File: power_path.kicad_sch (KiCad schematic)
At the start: 36 parts, among them J2 USB_C_Receptacle_USB2.0_16P, SW1 SW_SPST, U2 TPS631000DRLR, U3 TLV77018PDBVR, U4 TPS2116DRL, U5 USBLC6-2SC6, U6 USBLC6-2SC6, U7 BQ25302, U8 BQ27427YZFR

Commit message: random changes
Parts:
- SW1: value SW_SPST -> G-Switch SK-12E12-G060
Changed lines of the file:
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@@
 			)
 		)
-		(property "Datasheet" ""
+		(property "Datasheet" "https://www.ti.com/lit/ds/symlink/bq27427.pdf"
 			(at 246.38 121.92 0)
 			(hide yes)
@@
 			)
 		)
-		(property "Value" "SW_SPST"
+		(property "Value" "G-Switch SK-12E12-G060"
 			(at 203.2 102.87 0)
 			(show_name no)

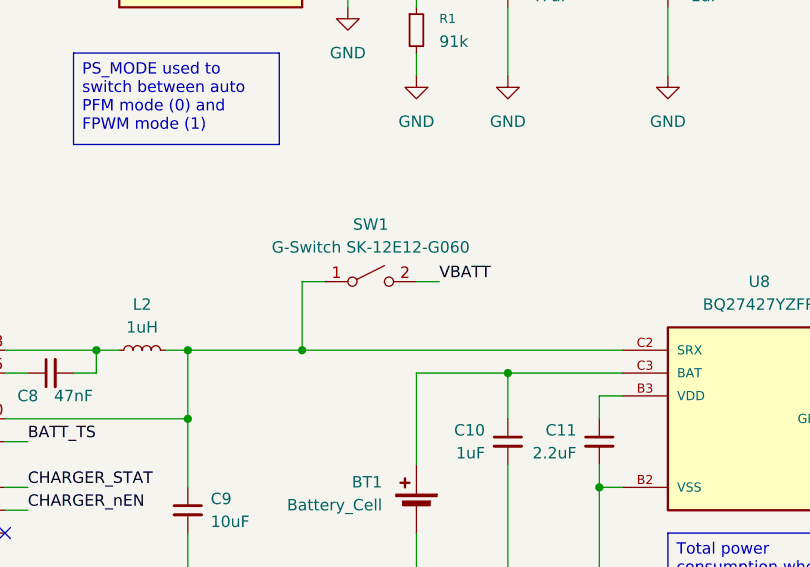
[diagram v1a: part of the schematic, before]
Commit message: rename custom libraries to custom, add easyeda2kicad integration
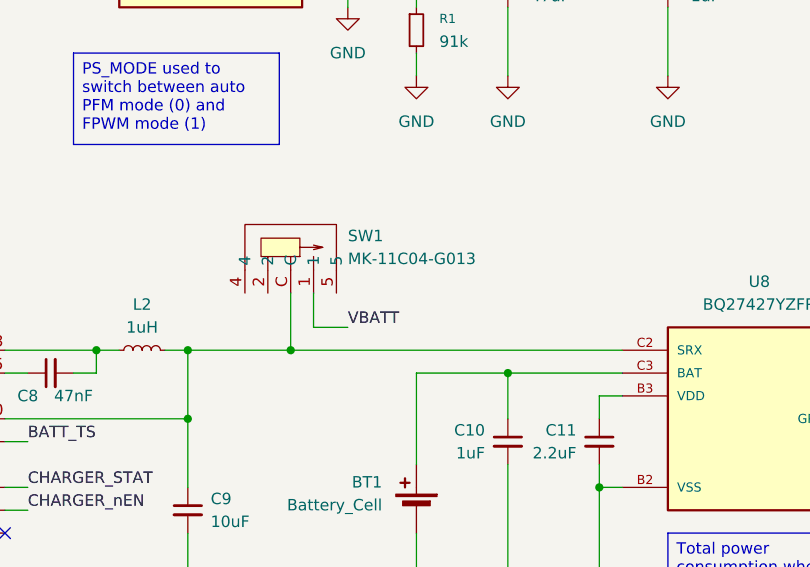
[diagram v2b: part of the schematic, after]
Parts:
- removed SW1: G-Switch SK-12E12-G060, footprints:SK-12E12-G060, symbol Switch:SW_SPST
- added SW1: MK-11C04-G013, custom:SW-SMD_MK-11C04-G013, symbol custom:MK-11C04-G013
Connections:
- net VBATT: now also SW1.1
- net at C9.1, L2.2, U7.10 (BAT)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: now also SW1.C
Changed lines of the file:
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@@
 	)
 	(junction
-		(at 139.7 177.8)
+		(at 194.31 114.3)
 		(diameter 0)
 		(color 0 0 0 0)
 	)
 	(junction
-		(at 99.06 73.66)
+		(at 139.7 177.8)
 		(diameter 0)
 		(color 0 0 0 0)
 	)
 	(junction
-		(at 195.58 114.3)
+		(at 99.06 73.66)
 		(diameter 0)
 		(color 0 0 0 0)
@@
 	(wire
 		(pts
-			(xy 195.58 106.68) (xy 198.12 106.68)
-		)
-		(stroke
-			(width 0)
-			(type default)
-		)
-	)
-	(wire
-		(pts
 			(xy 35.56 157.48) (xy 38.1 157.48)
 		)
@@
 	(wire
 		(pts
-			(xy 208.28 106.68) (xy 210.82 106.68)
+			(xy 236.22 63.5) (xy 243.84 63.5)
 		)
 		(stroke
@@
 	(wire
 		(pts
-			(xy 236.22 63.5) (xy 243.84 63.5)
+			(xy 99.06 71.12) (xy 99.06 73.66)
 		)
 		(stroke
@@
 	(wire
 		(pts
-			(xy 99.06 71.12) (xy 99.06 73.66)
+			(xy 35.56 147.32) (xy 38.1 147.32)
 		)
 		(stroke
@@
 	(wire
 		(pts
-			(xy 35.56 147.32) (xy 38.1 147.32)
+			(xy 68.58 76.2) (xy 68.58 78.74)
 		)
 		(stroke
@@
 	(wire
 		(pts
-			(xy 68.58 76.2) (xy 68.58 78.74)
+			(xy 170.18 68.58) (xy 172.72 68.58)
 		)
 		(stroke
@@
 	(wire
 		(pts
-			(xy 170.18 68.58) (xy 172.72 68.58)
+			(xy 124.46 139.7) (xy 124.46 142.24)
 		)
 		(stroke
@@
 	(wire
 		(pts
-			(xy 124.46 139.7) (xy 124.46 142.24)
+			(xy 196.85 107.95) (xy 196.85 111.76)
 		)
 		(stroke
@@
 	(wire
 		(pts
-			(xy 195.58 106.68) (xy 195.58 114.3)
+			(xy 194.31 107.95) (xy 194.31 114.3)
 		)
 		(stroke
@@
 	(wire
 		(pts
-			(xy 195.58 114.3) (xy 231.14 114.3)
-		)
-		(stroke
-			(width 0)
-			(type default)
-		)
-	)
-	(wire
-		(pts
 			(xy 66.04 68.58) (xy 68.58 68.58)
 		)
@@
 	(wire
 		(pts
-			(xy 182.88 114.3) (xy 195.58 114.3)
+			(xy 200.66 111.76) (xy 196.85 111.76)
+		)
+		(stroke
+			(width 0)
+			(type default)
+		)
+	)
+	(wire
+		(pts
+			(xy 182.88 114.3) (xy 194.31 114.3)
 		)
 		(stroke
@@
 	(wire
 		(pts
+			(xy 194.31 114.3) (xy 231.14 114.3)
+		)
+		(stroke
+			(width 0)
+			(type default)
+		)
+	)
+	(wire
+		(pts
 			(xy 264.16 116.84) (xy 261.62 116.84)
 		)
@@
 	)
 	(label "VBATT"
-		(at 210.82 106.68 0)
+		(at 200.66 111.76 0)
 		(effects
 			(font
@@
 	)
 	(symbol
+		(lib_id "custom:MK-11C04-G013")
+		(at 195.58 104.14 180)
+		(unit 1)
+		(body_style 1)
+		(exclude_from_sim no)
+		(in_bom yes)
+		(on_board yes)
+		(in_pos_files yes)
+		(dnp no)
+		(fields_autoplaced yes)
+		(property "Reference" "SW1"
+			(at 200.66 101.5999 0)
+			(show_name no)
+			(do_not_autoplace no)
+			(effects
+				(font
+					(size 1.27 1.27)
+				)
+				(justify right)
+			)
+		)
+		(property "Value" "MK-11C04-G013"
+			(at 200.66 104.1399 0)
+			(show_name no)
+			(do_not_autoplace no)
+			(effects
+				(font
+					(size 1.27 1.27)
+				)
+				(justify right)
+			)
+		)
+		(property "Footprint" "custom:SW-SMD_MK-11C04-G013"
+			(at 195.58 100.33 0)
+			(hide yes)
+			(show_name no)
+			(do_not_autoplace no)
+			(effects
+				(font
+					(size 1.27 1.27)
+				)
+			)
+		)
+		(property "Datasheet" "https://lcsc.com/product-detail/Toggle-Switches_G-Switch-MK-11C04-G013_C778185.html"
+			(at 195.58 97.79 0)
+			(hide yes)
+			(show_name no)
+			(do_not_autoplace no)
+			(effects
+				(font
+					(size 1.27 1.27)
+				)
+			)
+		)
+		(property "Description" ""
+			(at 195.58 104.14 0)
+			(hide yes)
+			(show_name no)
+			(do_not_autoplace no)
+			(effects
+				(font
+					(size 1.27 1.27)
+				)
+			)
+		)
+		(property "Manufacturer" "G-Switch(品赞)"
+			(at 195.58 95.25 0)
+			(hide yes)
+			(show_name no)
+			(do_not_autoplace no)
+			(effects
+				(font
+					(size 1.27 1.27)
+				)
+			)
+		)
+		(property "MPN" "MK-11C04-G013"
+			(at 195.58 92.71 0)
+			(hide yes)
+			(show_name no)
+			(do_not_autoplace no)
+			(effects
+				(font
+					(size 1.27 1.27)
+				)
+			)
+		)
+		(property "LCSC Part" "C778185"
+			(at 195.58 90.17 0)
+			(hide yes)
+			(show_name no)
+			(do_not_autoplace no)
+			(effects
+				(font
+					(size 1.27 1.27)
+				)
+			)
+		)
+		(property "LCSC" "C778185"
+			(at 195.58 85.09 0)
+			(hide yes)
+			(show_name no)
+			(do_not_autoplace no)
+			(effects
+				(font
+					(size 1.27 1.27)
+				)
+			)
+		)
+		(pin "5"
+		)
+		(pin "1"
+		)
+		(pin "4"
+		)
+		(pin "2"
+		)
+		(pin "C"
+		)
+		(instances
+			(project "pedal"
+				(path "/e2443317-b83f-4e66-ac79-3186c6d613f3/487ab5a8-1c1d-4a3e-8f62-a21afc38e9a3"
+					(reference "SW1")
+					(unit 1)
+				)
+			)
+		)
+	)
+	(symbol
 		(lib_id "Device:R_Small")
 		(at 274.32 121.92 90)
@@
 					(unit 1)
 				)
-			)
-		)
-	)
-	(symbol
-		(lib_id "Switch:SW_SPST")
-		(at 203.2 106.68 0)
-		(unit 1)
-		(body_style 1)
-		(exclude_from_sim no)
-		(in_bom yes)
-		(on_board yes)
-		(in_pos_files yes)
-		(dnp no)
-		(fields_autoplaced yes)
-		(property "Reference" "SW1"
-			(at 203.2 100.33 0)
-			(show_name no)
-			(do_not_autoplace no)
-			(effects
-				(font
-					(size 1.27 1.27)
-				)
-			)
-		)
-		(property "Value" "G-Switch SK-12E12-G060"
-			(at 203.2 102.87 0)
-			(show_name no)
-			(do_not_autoplace no)
-			(effects
-				(font
-					(size 1.27 1.27)
-				)
-			)
-		)
-		(property "Footprint" "footprints:SK-12E12-G060"
-			(at 203.2 106.68 0)
-			(hide yes)
-			(show_name no)
-			(do_not_autoplace no)
-			(effects
-				(font
-					(size 1.27 1.27)
-				)
-			)
-		)
-		(property "Datasheet" ""
-			(at 203.2 106.68 0)
-			(hide yes)
-			(show_name no)
-			(do_not_autoplace no)
-			(effects
-				(font
-					(size 1.27 1.27)
-				)
-			)
-		)
-		(property "Description" "Single Pole Single Throw (SPST) switch"
-			(at 203.2 106.68 0)
-			(hide yes)
-			(show_name no)
-			(do_not_autoplace no)
-			(effects
-				(font
-					(size 1.27 1.27)
-				)
-			)
-		)
-		(property "LCSC" "C22448008"
-			(at 203.2 106.68 0)
-			(hide yes)
-			(show_name no)
-			(do_not_autoplace no)
-			(effects
-				(font
-					(size 1.27 1.27)
-				)
-			)
-		)
-		(pin "1"
-		)
-		(pin "2"
-		)
-		(pin "3"
-		)
-		(pin "M"
-		)
-		(instances
-			(project "pedal"
-				(path "/e2443317-b83f-4e66-ac79-3186c6d613f3/487ab5a8-1c1d-4a3e-8f62-a21afc38e9a3"
-					(reference "SW1")
-					(unit 1)
-				)

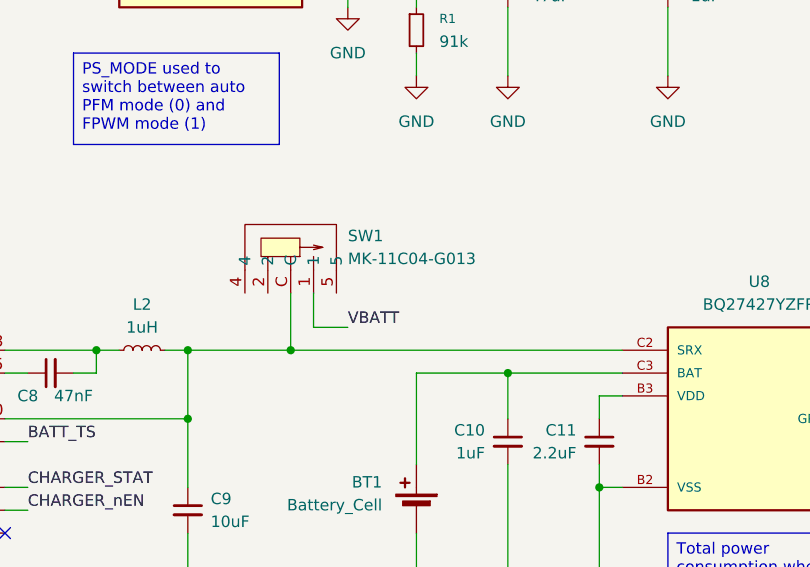
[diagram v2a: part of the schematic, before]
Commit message: move switch to be on grid
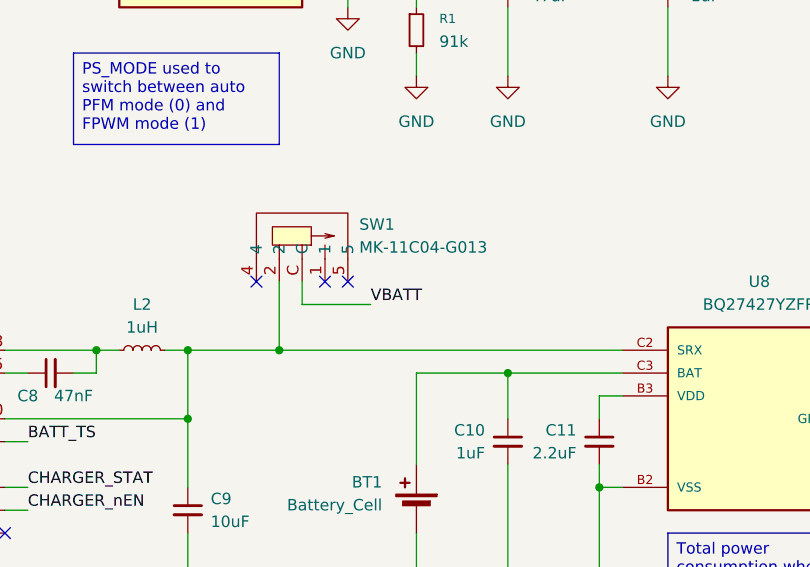
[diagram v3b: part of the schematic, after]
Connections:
- net VBATT: now also SW1.C; no longer SW1.1
- net at C9.1, L2.2, U7.10 (BAT)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: now also SW1.2; no longer SW1.C
- no-connect marks 2 -> 5
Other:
- moved on the sheet: SW1
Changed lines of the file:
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@@
 	)
 	(junction
-		(at 154.94 63.5)
+		(at 193.04 114.3)
 		(diameter 0)
 		(color 0 0 0 0)
 	)
 	(junction
-		(at 208.28 63.5)
+		(at 154.94 63.5)
 		(diameter 0)
 		(color 0 0 0 0)
 	)
 	(junction
-		(at 149.86 142.24)
+		(at 208.28 63.5)
 		(diameter 0)
 		(color 0 0 0 0)
 	)
 	(junction
-		(at 172.72 114.3)
+		(at 149.86 142.24)
 		(diameter 0)
 		(color 0 0 0 0)
 	)
 	(junction
-		(at 194.31 114.3)
+		(at 172.72 114.3)
 		(diameter 0)
 		(color 0 0 0 0)
@@
 		(at 162.56 134.62)
 	)
+	(no_connect
+		(at 190.5 106.68)
+	)
+	(no_connect
+		(at 200.66 106.68)
+	)
+	(no_connect
+		(at 198.12 106.68)
+	)
 	(wire
 		(pts
@@
 	(wire
 		(pts
-			(xy 196.85 107.95) (xy 196.85 111.76)
+			(xy 195.58 106.68) (xy 195.58 109.22)
 		)
 		(stroke
@@
 	(wire
 		(pts
-			(xy 194.31 107.95) (xy 194.31 114.3)
+			(xy 193.04 106.68) (xy 193.04 114.3)
 		)
 		(stroke
@@
 	(wire
 		(pts
-			(xy 200.66 111.76) (xy 196.85 111.76)
+			(xy 203.2 109.22) (xy 195.58 109.22)
 		)
 		(stroke
@@
 	(wire
 		(pts
-			(xy 182.88 114.3) (xy 194.31 114.3)
+			(xy 182.88 114.3) (xy 193.04 114.3)
 		)
 		(stroke
@@
 	(wire
 		(pts
+			(xy 193.04 114.3) (xy 231.14 114.3)
+		)
+		(stroke
+			(width 0)
+			(type default)
+		)
+	)
+	(wire
+		(pts
 			(xy 124.46 132.08) (xy 124.46 134.62)
 		)
@@
 	(wire
 		(pts
-			(xy 194.31 114.3) (xy 231.14 114.3)
-		)
-		(stroke
-			(width 0)
-			(type default)
-		)
-	)
-	(wire
-		(pts
 			(xy 264.16 116.84) (xy 261.62 116.84)
 		)
@@
 	)
 	(label "VBATT"
-		(at 200.66 111.76 0)
+		(at 203.2 109.22 0)
 		(effects
 			(font
@@
 	(symbol
 		(lib_id "custom:MK-11C04-G013")
-		(at 195.58 104.14 180)
+		(at 196.85 102.87 180)
 		(unit 1)
 		(body_style 1)
@@
 		(fields_autoplaced yes)
 		(property "Reference" "SW1"
-			(at 200.66 101.5999 0)
+			(at 201.93 100.3299 0)
 			(show_name no)
 			(do_not_autoplace no)
@@
 		)
 		(property "Value" "MK-11C04-G013"
-			(at 200.66 104.1399 0)
+			(at 201.93 102.8699 0)
 			(show_name no)
 			(do_not_autoplace no)
@@
 		)
 		(property "Footprint" "custom:SW-SMD_MK-11C04-G013"
-			(at 195.58 100.33 0)
+			(at 196.85 99.06 0)
 			(hide yes)
 			(show_name no)
@@
 		)
 		(property "Datasheet" "https://lcsc.com/product-detail/Toggle-Switches_G-Switch-MK-11C04-G013_C778185.html"
-			(at 195.58 97.79 0)
+			(at 196.85 96.52 0)
 			(hide yes)
 			(show_name no)
@@
 		)
 		(property "Description" ""
-			(at 195.58 104.14 0)
+			(at 196.85 102.87 0)
 			(hide yes)
 			(show_name no)
@@
 		)
 		(property "Manufacturer" "G-Switch(品赞)"
-			(at 195.58 95.25 0)
+			(at 196.85 93.98 0)
 			(hide yes)
 			(show_name no)
@@
 		)
 		(property "MPN" "MK-11C04-G013"
-			(at 195.58 92.71 0)
+			(at 196.85 91.44 0)
 			(hide yes)
 			(show_name no)
@@
 		)
 		(property "LCSC Part" "C778185"
-			(at 195.58 90.17 0)
+			(at 196.85 88.9 0)
 			(hide yes)
 			(show_name no)
@@
 		)
 		(property "LCSC" "C778185"
-			(at 195.58 85.09 0)
+			(at 196.85 83.82 0)
 			(hide yes)
 			(show_name no)

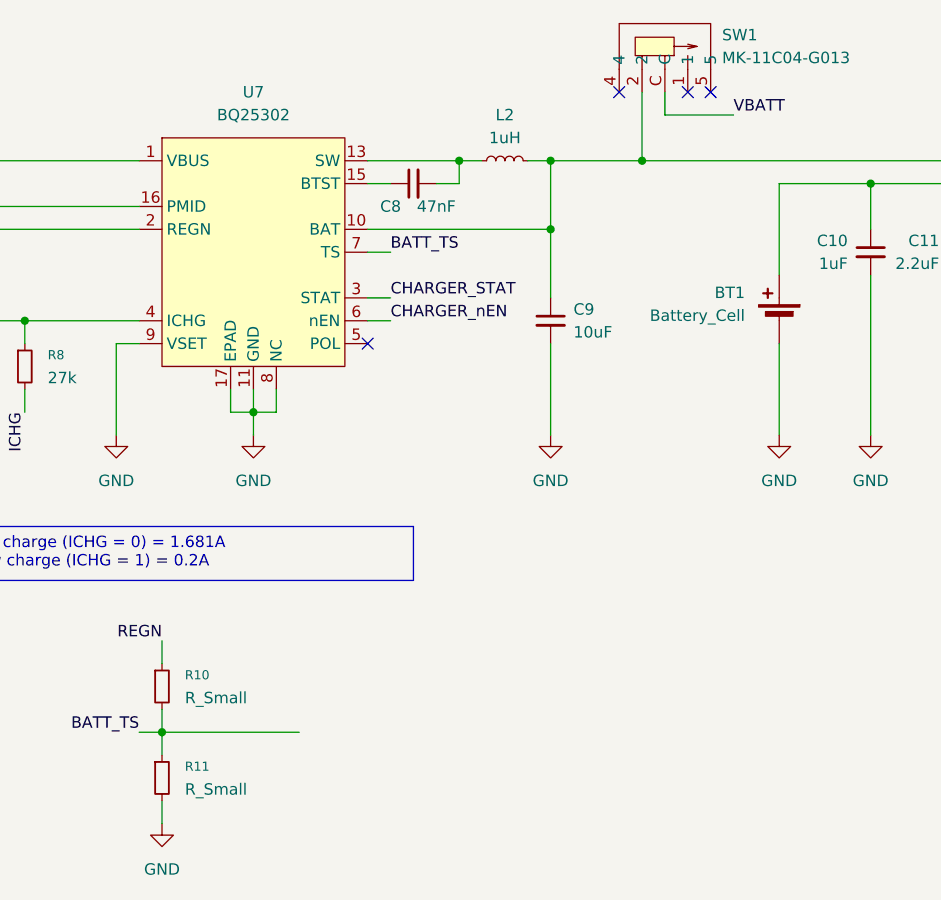
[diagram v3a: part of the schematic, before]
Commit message: add thermistor biasing resistors
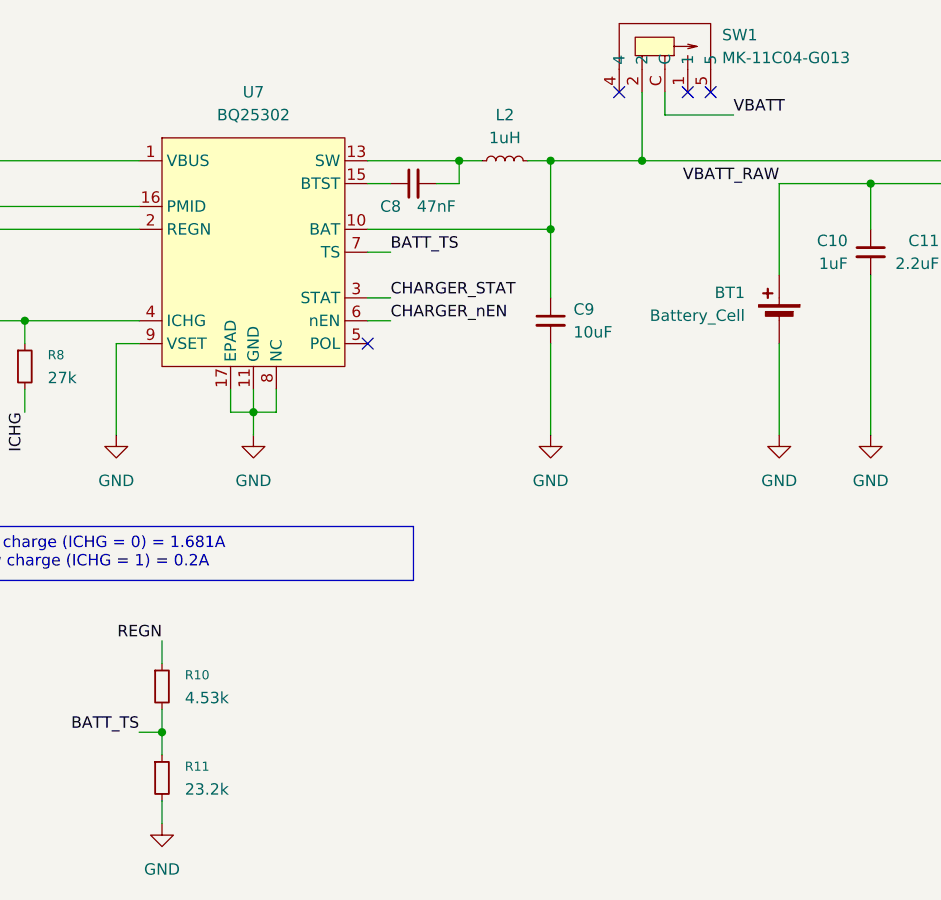
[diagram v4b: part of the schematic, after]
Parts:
- R10: value R_Small -> 4.53k; footprint (none) -> Resistor_SMD:R_0402_1005Metric; LCSC (none) -> C79537
- R11: value R_Small -> 23.2k; footprint (none) -> Resistor_SMD:R_0402_1005Metric; LCSC (none) -> C25873
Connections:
- net VBATT_RAW: now reaches BT1.1 (+), C10.1, U8.C3 (BAT)
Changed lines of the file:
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@@
 	(wire
 		(pts
-			(xy 139.7 177.8) (xy 154.94 177.8)
-		)
-		(stroke
-			(width 0)
-			(type default)
-		)
-	)
-	(wire
-		(pts
 			(xy 104.14 137.16) (xy 104.14 144.78)
 		)
@@
 		)
 	)
+	(label "VBATT_RAW"
+		(at 208.28 116.84 180)
+		(effects
+			(font
+				(size 1.27 1.27)
+			)
+			(justify right bottom)
+		)
+	)
 	(label "SDA"
 		(at 38.1 162.56 0)
@@
 			)
 		)
-		(property "Value" "R_Small"
+		(property "Value" "23.2k"
 			(at 142.24 184.1499 0)
 			(show_name no)
@@
 			)
 		)
-		(property "Footprint" ""
+		(property "Footprint" "Resistor_SMD:R_0402_1005Metric"
 			(at 139.7 182.88 0)
 			(hide yes)
@@
 			)
 		)
+		(property "LCSC" "C25873"
+			(at 139.7 182.88 0)
+			(hide yes)
+			(show_name no)
+			(do_not_autoplace no)
+			(effects
+				(font
+					(size 1.27 1.27)
+				)
+			)
+		)
 		(pin "1"
 		)
@@
 			)
 		)
-		(property "Value" "R_Small"
+		(property "Value" "4.53k"
 			(at 142.24 173.9899 0)
 			(show_name no)
@@
 			)
 		)
-		(property "Footprint" ""
+		(property "Footprint" "Resistor_SMD:R_0402_1005Metric"
 			(at 139.7 172.72 0)
 			(hide yes)
@@
 			(at 139.7 172.72 0)
 			(hide yes)
+			(show_name no)
+			(do_not_autoplace no)
+			(effects
+				(font
+					(size 1.27 1.27)
+				)
+			)
+		)
+		(property "LCSC" "C79537"
+			(at 139.7 172.72 0)
+			(hide yes)

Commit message: add battery connector
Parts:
- added J1: Battery, symbol Connector_Generic_MountingPin:Conn_01x04_MountingPin
- added JP1: (no value), Jumper:SolderJumper-2_P1.3mm_Bridged2Bar_RoundedPad1.0x1.5mm, symbol Jumper:SolderJumper_2_Bridged
- added R14: 10k, Resistor_SMD:R_0402_1005Metric, symbol Device:R_Small
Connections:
- net BATT_TS: now also J1.3 (Pin_3), JP1.1 (A)
- net GND: now also J1.1 (Pin_1), J1.2 (Pin_2), R14.2
- net VBATT_RAW: now also J1.4 (Pin_4)
- new net: JP1.2 (B), R14.1
- no-connect marks 5 -> 6
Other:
- moved on the sheet: R10, R11

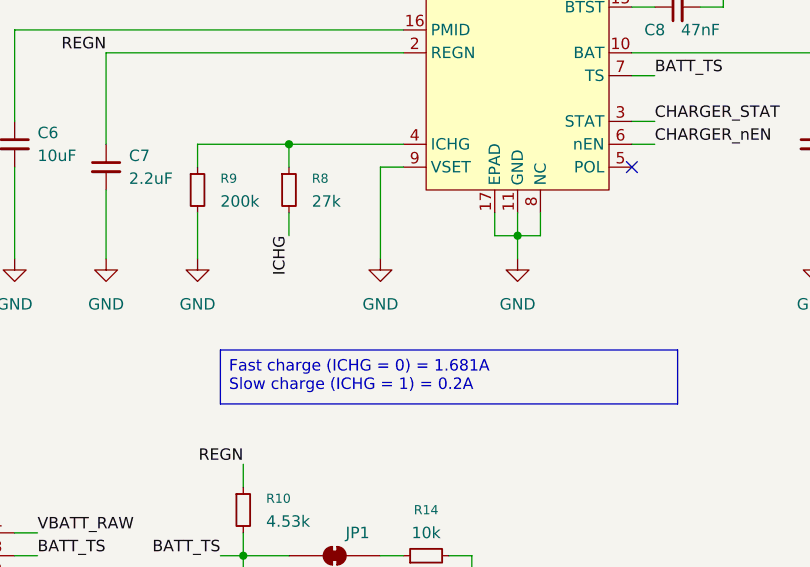
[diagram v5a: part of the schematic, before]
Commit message: update fast charge current
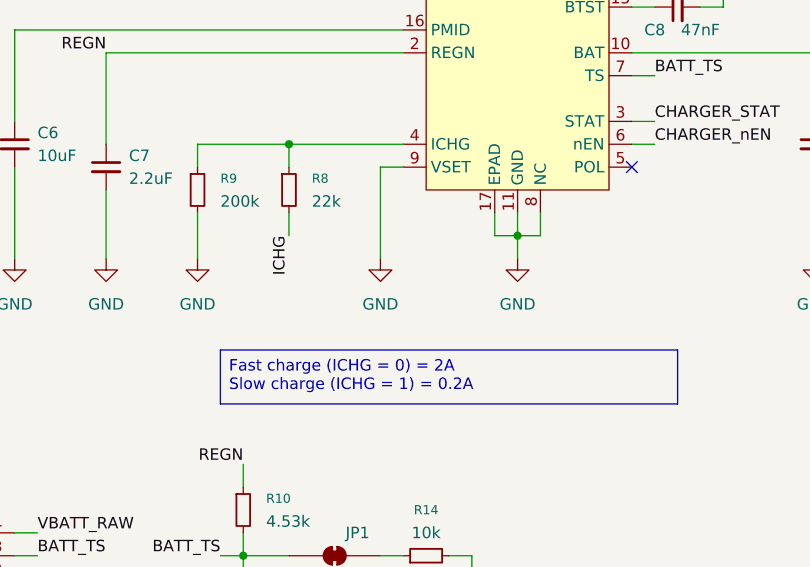
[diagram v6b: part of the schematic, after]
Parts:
- R8: value 27k -> 22k; LCSC C25771 -> C25768
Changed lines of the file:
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@@
 		)
 	)
-	(text_box "Fast charge (ICHG = 0) = 1.681A\nSlow charge (ICHG = 1) = 0.2A"
+	(text_box "Fast charge (ICHG = 0) = 2A\nSlow charge (ICHG = 1) = 0.2A"
 		(exclude_from_sim no)
 		(at 116.84 154.94 0)
@@
 	(wire
 		(pts
+			(xy 35.56 152.4) (xy 38.1 152.4)
+		)
+		(stroke
+			(width 0)
+			(type default)
+		)
+	)
+	(wire
+		(pts
 			(xy 218.44 60.96) (xy 218.44 63.5)
 		)
@@
 	(wire
 		(pts
-			(xy 35.56 152.4) (xy 38.1 152.4)
-		)
-		(stroke
-			(width 0)
-			(type default)
-		)
-	)
-	(wire
-		(pts
 			(xy 35.56 167.64) (xy 38.1 167.64)
 		)
@@
 		)
 	)
-	(label "CHARGER_nEN"
-		(at 38.1 152.4 0)
-		(effects
-			(font
-				(size 1.27 1.27)
-			)
-			(justify left bottom)
-		)
-	)
 	(label "BATT_TS"
 		(at 96.52 177.8 0)
@@
 		)
 	)
+	(label "CHARGER_nEN"
+		(at 38.1 152.4 0)
+		(effects
+			(font
+				(size 1.27 1.27)
+			)
+			(justify left bottom)
+		)
+	)
 	(label "BATT_TS"
 		(at 165.1 124.46 0)
@@
 			)
 		)
-		(property "Value" "27k"
+		(property "Value" "22k"
 			(at 127 138.4299 0)
 			(show_name no)
@@
 			)
 		)
-		(property "LCSC" "C25771"
+		(property "LCSC" "C25768"
 			(at 124.46 137.16 0)
 			(hide yes)
